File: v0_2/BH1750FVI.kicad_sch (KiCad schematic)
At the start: 8 parts, among them IC2 BH1750FVI-TR

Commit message: schematic for enviro done
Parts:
- removed JP1: Jumper_2_Open, symbol Jumper:Jumper_2_Open
- added JP1: SolderJumper_2_Open, symbol Jumper:SolderJumper_2_Open
- IC2: footprint WSOF6 -> BH1750:WSOF6
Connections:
- net +3.3V: now also JP1.1 (A)
- net at IC2.2 (ADDR), R8.1: now also JP1.2 (B)
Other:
- note added: "Color Sensor"
- moved on the sheet: R9

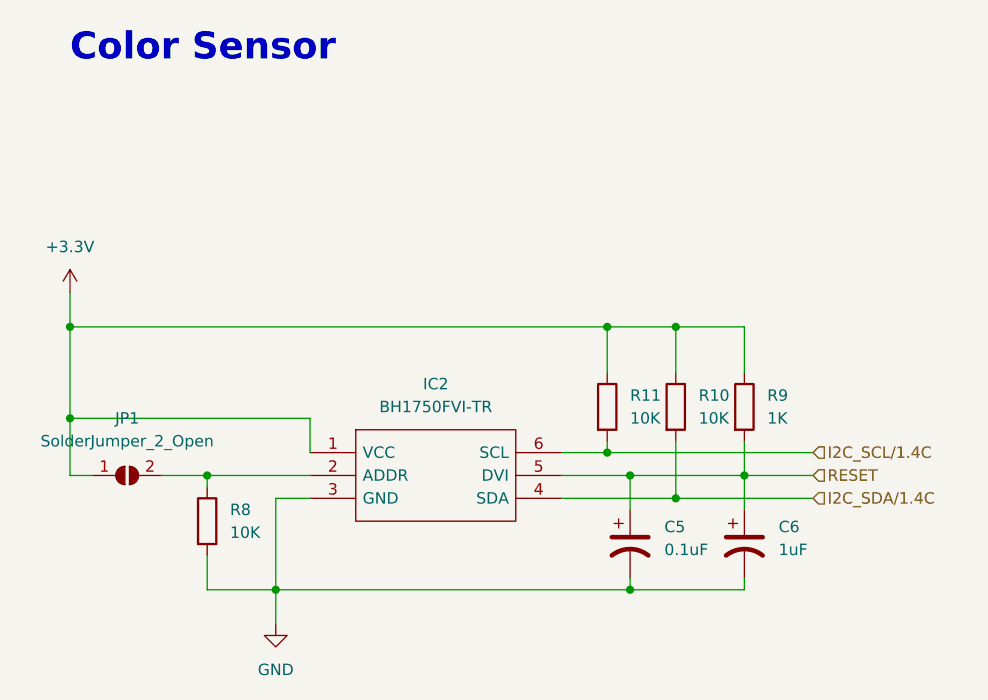
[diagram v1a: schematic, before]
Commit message: all part are added
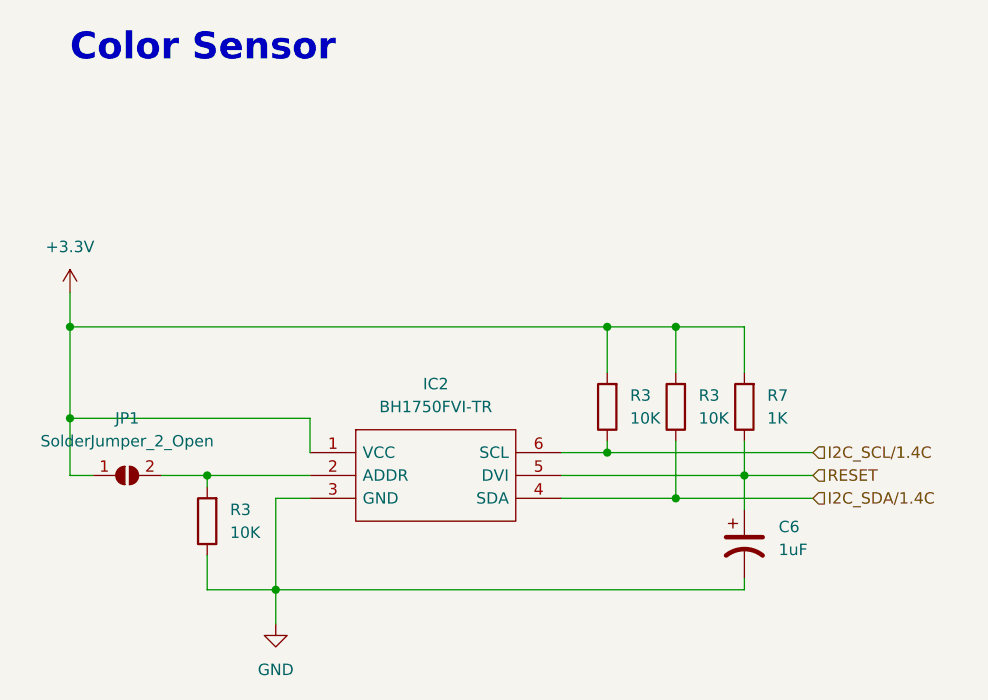
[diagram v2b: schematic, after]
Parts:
- removed C5: 0.1uF, symbol Device:C_Polarized_US
- removed R10, R11, R8: 10K, symbol Device:R
- removed R9: 1K, symbol Device:R
- added R3 (x3): 10K, Resistor_SMD:R_0603_1608Metric, symbol Device:R
- added R7: 1K, Resistor_SMD:R_0603_1608Metric, symbol Device:R
- C6: footprint (none) -> Capacitor_SMD:C_0603_1608Metric; Manufacture (none) -> CL10A105KO8NNNC
- JP1: footprint (none) -> Jumper:SolderJumper-2_P1.3mm_Open_TrianglePad1.0x1.5mm
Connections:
- net +3.3V: now also R3.2, R3.2, R7.2
- net GND: now also R3.1
- net I2C_SCL/1.4C: now also R3.1
- net I2C_SDA/1.4C: now also R3.1
- net RESET: now also R7.1
- net at IC2.2 (ADDR), JP1.2 (B): now also R3.2

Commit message: for quoate
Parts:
- removed R3 (x2): 10K, Resistor_SMD:R_0603_1608Metric, symbol Device:R
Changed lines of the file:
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@@
 (kicad_sch (version 20230121) (generator eeschema)
   (paper "A4")
-  (junction (at 157.48 90.17) (diameter 0) (color 0 0 0 0)
-  )
-  (junction (at 157.48 76.2) (diameter 0) (color 0 0 0 0)
-  )
-  (junction (at 165.1 76.2) (diameter 0) (color 0 0 0 0)
-  )
-  (junction (at 165.1 95.25) (diameter 0) (color 0 0 0 0)
-  )
   (junction (at 97.79 86.36) (diameter 0) (color 0 0 0 0)
   )
@@
     (stroke (width 0) (type default))
   )
-  (wire (pts (xy 152.4 95.25) (xy 165.1 95.25))
-    (stroke (width 0) (type default))
-  )
-  (wire (pts (xy 172.72 76.2) (xy 165.1 76.2))
+  (wire (pts (xy 152.4 95.25) (xy 180.34 95.25))
     (stroke (width 0) (type default))
   )
@@
     (stroke (width 0) (type default))
   )
-  (wire (pts (xy 157.48 76.2) (xy 97.79 76.2))
-    (stroke (width 0) (type default))
-  )
-  (wire (pts (xy 152.4 90.17) (xy 157.48 90.17))
-    (stroke (width 0) (type default))
-  )
-  (wire (pts (xy 165.1 76.2) (xy 165.1 81.28))
+  (wire (pts (xy 97.79 76.2) (xy 172.72 76.2))
+    (stroke (width 0) (type default))
+  )
+  (wire (pts (xy 152.4 90.17) (xy 180.34 90.17))
     (stroke (width 0) (type default))
   )
@@
     (stroke (width 0) (type default))
   )
-  (wire (pts (xy 165.1 76.2) (xy 157.48 76.2))
-    (stroke (width 0) (type default))
-  )
-  (wire (pts (xy 165.1 88.9) (xy 165.1 95.25))
-    (stroke (width 0) (type default))
-  )
   (wire (pts (xy 172.72 105.41) (xy 172.72 104.14))
     (stroke (width 0) (type default))
@@
     (stroke (width 0) (type default))
   )
-  (wire (pts (xy 165.1 95.25) (xy 180.34 95.25))
-    (stroke (width 0) (type default))
-  )
   (wire (pts (xy 100.33 92.71) (xy 97.79 92.71))
     (stroke (width 0) (type default))
@@
     (stroke (width 0) (type default))
   )
-  (wire (pts (xy 157.48 76.2) (xy 157.48 81.28))
-    (stroke (width 0) (type default))
-  )
   (wire (pts (xy 172.72 92.71) (xy 180.34 92.71))
     (stroke (width 0) (type default))
   )
-  (wire (pts (xy 157.48 88.9) (xy 157.48 90.17))
-    (stroke (width 0) (type default))
-  )
   (wire (pts (xy 120.65 105.41) (xy 120.65 109.22))
-    (stroke (width 0) (type default))
-  )
-  (wire (pts (xy 157.48 90.17) (xy 180.34 90.17))
     (stroke (width 0) (type default))
   )
@@
     )
   )
-  (symbol (lib_id "Device:R") (at 165.1 85.09 180) (unit 1)
-    (in_bom yes) (on_board yes) (dnp no) (fields_autoplaced)
-    (property "Reference" "R3" (at 167.64 83.82 0)
-      (effects (font (size 1.27 1.27)) (justify right))
-    )
-    (property "Value" "10K" (at 167.64 86.36 0)
-      (effects (font (size 1.27 1.27)) (justify right))
-    )
-    (property "Footprint" "Resistor_SMD:R_0603_1608Metric" (at 166.878 85.09 90)
-      (effects (font (size 1.27 1.27)) hide)
-    )
-    (property "Datasheet" "~" (at 165.1 85.09 0)
-      (effects (font (size 1.27 1.27)) hide)
-    )
-    (property "Manufacturer_Part_Number" "0603WAF1002T5E" (at 165.1 85.09 90)
+  (symbol (lib_id "Device:R") (at 172.72 85.09 180) (unit 1)
+    (in_bom yes) (on_board yes) (dnp no) (fields_autoplaced)
+    (property "Reference" "R7" (at 175.26 83.82 0)
+      (effects (font (size 1.27 1.27)) (justify right))
+    )
+    (property "Value" "1K" (at 175.26 86.36 0)
+      (effects (font (size 1.27 1.27)) (justify right))
+    )
+    (property "Footprint" "Resistor_SMD:R_0603_1608Metric" (at 174.498 85.09 90)
+      (effects (font (size 1.27 1.27)) hide)
+    )
+    (property "Datasheet" "~" (at 172.72 85.09 0)
+      (effects (font (size 1.27 1.27)) hide)
+    )
+    (property "Manufacturer_Part_Number" "0603WAF1001T5E" (at 172.72 85.09 90)
+      (effects (font (size 1.27 1.27)) hide)
+    )
+    (pin "1")
+    (pin "2")
+    (instances
+      (project "v0_2"
+        (path "/678523e5-508b-4706-b0e0-f17e466a8d09"
+          (reference "R7") (unit 1)
+        )
+        (path "/678523e5-508b-4706-b0e0-f17e466a8d09/b4cf97a4-fc8e-43ca-87b5-9f012553953c"
+          (reference "R8") (unit 1)
+        )
+      )
+    )
+  )
+  (symbol (lib_id "Device:R") (at 113.03 97.79 180) (unit 1)
+    (in_bom yes) (on_board yes) (dnp no) (fields_autoplaced)
+    (property "Reference" "R3" (at 115.57 96.52 0)
+      (effects (font (size 1.27 1.27)) (justify right))
+    )
+    (property "Value" "10K" (at 115.57 99.06 0)
+      (effects (font (size 1.27 1.27)) (justify right))
+    )
+    (property "Footprint" "Resistor_SMD:R_0603_1608Metric" (at 114.808 97.79 90)
+      (effects (font (size 1.27 1.27)) hide)
+    )
+    (property "Datasheet" "~" (at 113.03 97.79 0)
+      (effects (font (size 1.27 1.27)) hide)
+    )
+    (property "Manufacturer_Part_Number" "0603WAF1002T5E" (at 113.03 97.79 90)
       (effects (font (size 1.27 1.27)) hide)
     )
@@
         )
         (path "/678523e5-508b-4706-b0e0-f17e466a8d09/b4cf97a4-fc8e-43ca-87b5-9f012553953c"
-          (reference "R14") (unit 1)
-        )
-      )
-    )
-  )
-  (symbol (lib_id "Device:R") (at 172.72 85.09 180) (unit 1)
-    (in_bom yes) (on_board yes) (dnp no) (fields_autoplaced)
-    (property "Reference" "R7" (at 175.26 83.82 0)
-      (effects (font (size 1.27 1.27)) (justify right))
-    )
-    (property "Value" "1K" (at 175.26 86.36 0)
-      (effects (font (size 1.27 1.27)) (justify right))
-    )
-    (property "Footprint" "Resistor_SMD:R_0603_1608Metric" (at 174.498 85.09 90)
-      (effects (font (size 1.27 1.27)) hide)
-    )
-    (property "Datasheet" "~" (at 172.72 85.09 0)
-      (effects (font (size 1.27 1.27)) hide)
-    )
-    (property "Manufacturer_Part_Number" "0603WAF1001T5E" (at 172.72 85.09 90)
-      (effects (font (size 1.27 1.27)) hide)
-    )
-    (pin "1")
-    (pin "2")
-    (instances
-      (project "v0_2"
-        (path "/678523e5-508b-4706-b0e0-f17e466a8d09"
-          (reference "R7") (unit 1)
-        )
-        (path "/678523e5-508b-4706-b0e0-f17e466a8d09/b4cf97a4-fc8e-43ca-87b5-9f012553953c"
-          (reference "R8") (unit 1)
-        )
-      )
-    )
-  )
-  (symbol (lib_id "Device:R") (at 113.03 97.79 180) (unit 1)
-    (in_bom yes) (on_board yes) (dnp no) (fields_autoplaced)
-    (property "Reference" "R3" (at 115.57 96.52 0)
-      (effects (font (size 1.27 1.27)) (justify right))
-    )
-    (property "Value" "10K" (at 115.57 99.06 0)
-      (effects (font (size 1.27 1.27)) (justify right))
-    )
-    (property "Footprint" "Resistor_SMD:R_0603_1608Metric" (at 114.808 97.79 90)
-      (effects (font (size 1.27 1.27)) hide)
-    )
-    (property "Datasheet" "~" (at 113.03 97.79 0)
-      (effects (font (size 1.27 1.27)) hide)
-    )
-    (property "Manufacturer_Part_Number" "0603WAF1002T5E" (at 113.03 97.79 90)
-      (effects (font (size 1.27 1.27)) hide)
-    )
-    (pin "1")
-    (pin "2")
-    (instances
-      (project "v0_2"
-        (path "/678523e5-508b-4706-b0e0-f17e466a8d09"
-          (reference "R3") (unit 1)
-        )
-        (path "/678523e5-508b-4706-b0e0-f17e466a8d09/b4cf97a4-fc8e-43ca-87b5-9f012553953c"
           (reference "R20") (unit 1)
         )
@@
         )
       )
-    )
-  )
-  (symbol (lib_id "Device:R") (at 157.48 85.09 180) (unit 1)
-    (in_bom yes) (on_board yes) (dnp no) (fields_autoplaced)
-    (property "Reference" "R3" (at 160.02 83.82 0)
-      (effects (font (size 1.27 1.27)) (justify right))
-    )
-    (property "Value" "10K" (at 160.02 86.36 0)
-      (effects (font (size 1.27 1.27)) (justify right))
-    )
-    (property "Footprint" "Resistor_SMD:R_0603_1608Metric" (at 159.258 85.09 90)
-      (effects (font (size 1.27 1.27)) hide)
-    )
-    (property "Datasheet" "~" (at 157.48 85.09 0)
-      (effects (font (size 1.27 1.27)) hide)
-    )
-    (property "Manufacturer_Part_Number" "0603WAF1002T5E" (at 157.48 85.09 90)
-      (effects (font (size 1.27 1.27)) hide)
-    )
-    (pin "1")
-    (pin "2")
-    (instances
-      (project "v0_2"
-        (path "/678523e5-508b-4706-b0e0-f17e466a8d09"
-          (reference "R3") (unit 1)
-        )
-        (path "/678523e5-508b-4706-b0e0-f17e466a8d09/b4cf97a4-fc8e-43ca-87b5-9f012553953c"
-          (reference "R13") (unit 1)
-        )
-      )
